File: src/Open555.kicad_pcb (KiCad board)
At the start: 2 copper layers, 92.3 x 46.7 mm, 83 parts, among them J1 Conn_01x05_Pin, Q1 PNP, Q10 NPN, Q11 NPN, Q12 NPN, Q13 PNP, Q14 PNP, Q15 NPN, Q16 NPN, Q17 PNP, Q18 PNP, Q19 NPN, Q2 PNP, Q20 NPN, Q21 NPN, Q22 NPN, Q3 PNP, Q4 PNP, Q5 PNP, Q6 PNP, Q7 PNP, Q8 NPN, Q9 NPN, SW1 SW_Push

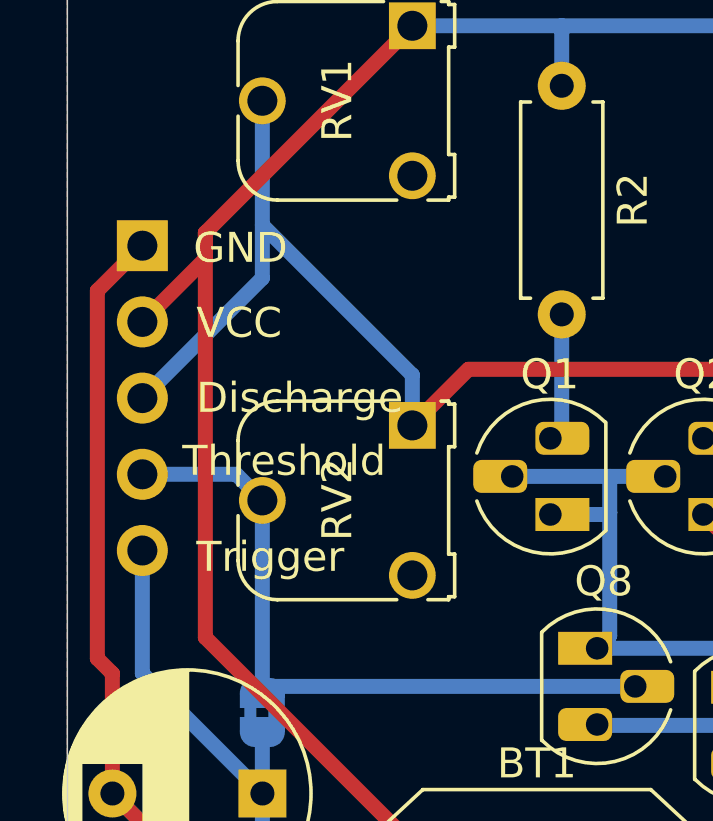
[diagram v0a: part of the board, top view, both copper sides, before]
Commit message: Add 3D models
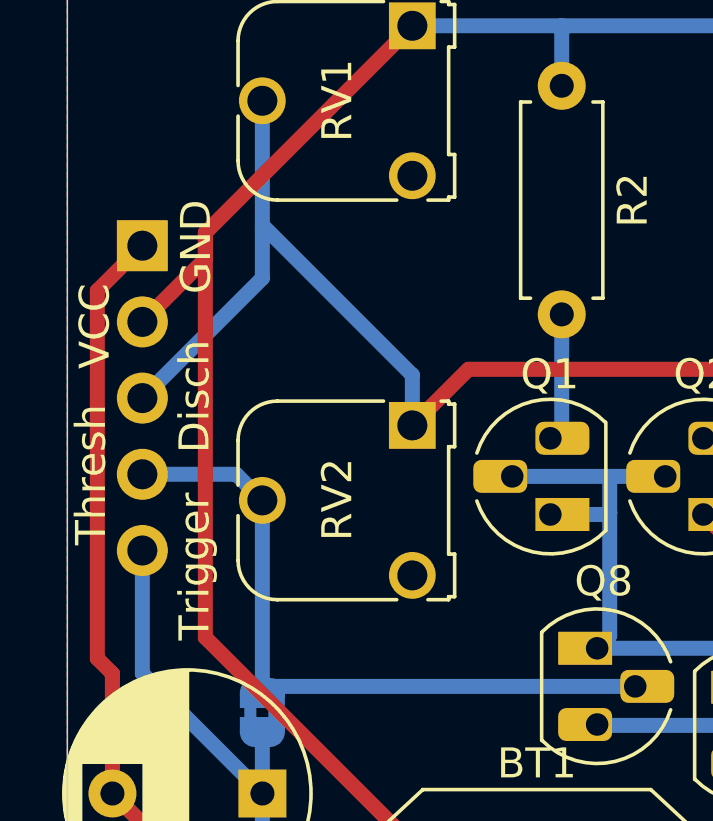
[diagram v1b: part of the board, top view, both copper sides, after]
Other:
- board text added: "Disch"
- board text added: "Thresh"
- board text removed: "Discharge"
- board text removed: "Threshold"
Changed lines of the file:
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@@
 		)
 		(embedded_fonts no)
-		(model "${KICAD9_3DMODEL_DIR}/Potentiometer_THT.3dshapes/Potentiometer_Runtron_RM-065_Vertical.wrl"
+		(model "${KIPRJMOD}/../models/Trim_Potentiometer_502.step"
 			(offset
-				(xyz 0 0 0)
+				(xyz 2.5 -2.8 6)
 			)
 			(scale
@@
 			)
 			(rotate
-				(xyz 0 0 0)
+				(xyz -0 -0 -180)
 			)
 		)
@@
 		)
 		(embedded_fonts no)
-		(model "${KICAD9_3DMODEL_DIR}/Potentiometer_THT.3dshapes/Potentiometer_Runtron_RM-065_Vertical.wrl"
+		(model "${KIPRJMOD}/../models/Trim_Potentiometer_502.step"
 			(offset
-				(xyz 0 0 0)
+				(xyz 2.5 -2.8 6)
 			)
 			(scale
@@
 			)
 			(rotate
-				(xyz 0 0 0)
+				(xyz -0 -0 -180)
 			)
 		)
@@
 		)
 		(embedded_fonts no)
-		(model "${KICAD9_3DMODEL_DIR}/Battery.3dshapes/BatteryHolder_Multicomp_BC-2001_1x2032.wrl"
+		(model "${KICAD9_3DMODEL_DIR}/Battery.3dshapes/BatteryHolder_Keystone_3034_1x20mm.step"
 			(offset
 				(xyz 0 0 0)
@@
 			)
 			(rotate
-				(xyz 0 0 0)
+				(xyz -0 -0 -180)
 			)
 		)
@@
 	)
 	(gr_text "VCC"
-		(at 23.4 134 0)
+		(at 20.6 134.95 90)
 		(layer "F.SilkS")
 		(effects
@@
 		)
 	)
-	(gr_text "Threshold"
-		(at 22.93 138.6 0)
+	(gr_text "Thresh"
+		(at 20.475 140.825 90)
 		(layer "F.SilkS")
 		(effects
@@
 	)
 	(gr_text "Trigger"
-		(at 23.4 141.8 0)
+		(at 23.925 144 90)
 		(layer "F.SilkS")
 		(effects
@@
 		)
 	)
-	(gr_text "Discharge"
-		(at 23.4 136.5 0)
+	(gr_text "Disch"
+		(at 23.925 137.75 90)
 		(layer "F.SilkS")
 		(effects
@@
 	)
 	(gr_text "GND"
-		(at 23.3 131.5 0)
+		(at 23.975 132.45 90)
 		(layer "F.SilkS")
 		(effects
@@
 	)
 	(gr_text "Source here!"
-		(at 97.365 168.335 0)
+		(at 97.075 168.325 0)
 		(layer "B.SilkS")
 		(effects

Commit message: Final revision
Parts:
- added G***: LOGO, LOGO, F.Cu at (149.2, 95.1)
- D1: footprint LED_THT:LED_D3.0mm -> LED_THT:LED_D5.0mm
- R10, R11, R12, R14, R17, R18, R2, R4, R5, R6: value R -> 4.7k
- R13: value R -> 10k
- R16: value R -> 100k
- R3, R7, R8: value R -> 100
- moved G*** 98.3 mm to (169.3, 95.4)
- moved G*** 98.3 mm to (148.3, 92.5)
- moved G*** 98.3 mm to (141.4, 100.7)
- moved G*** 98.3 mm to (169.1, 103.7)
- moved G*** 98.3 mm to (151.6, 98.5)
- moved G*** 98.3 mm to (179.3, 101.1)
- moved G*** 98.3 mm to (174.2, 102.4)
- moved G*** 98.3 mm to (132.4, 90.6)
- moved G*** 98.3 mm to (179.4, 109.0)
- moved R3 98.3 mm to (127.8, 75.1)
- moved BT1 98.3 mm to (119.1, 109.2)
- moved G*** 98.3 mm to (160.2, 104.5)
- moved G*** 98.3 mm to (185.8, 102.4)
- moved G*** 98.3 mm to (120.9, 95.1)
- moved G*** 98.3 mm to (127.8, 78.9)
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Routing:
- net Net-(Q12-E): track 16.1 -> 18.9 mm
- net GND: track 226.6 -> 227.6 mm, vias 1 -> 7
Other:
- board size 92.3 x 46.7 mm -> 92.6 x 46.8 mm
